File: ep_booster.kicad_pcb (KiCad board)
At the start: 2 copper layers, 37.7 x 25.1 mm, 28 parts, among them J1 TB002-500-04BE, Q1 MMBF5457, Q2 BC849C, SW1 SW_DIP_x02

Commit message: libs and pcb design update (2)
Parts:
- Q1, Q2, R1, R10, R11, R12, R13, R14, R16, R2, R3, R4, R5, R6, R7, R8, R9: moved to B.Cu
- moved R12 30.5 mm to (212.4, 89.4), turned to -90 degrees
- moved R16 27.1 mm to (209.8, 89.4), turned to -90 degrees
- moved R6 26.6 mm to (212.4, 95.4), turned to -90 degrees
- moved R4 25.2 mm to (197.6, 83.2), turned to 0 degrees
- moved R9 24.0 mm to (200.0, 93.0)
- moved C5 21.2 mm to (208.5, 85.0)
- moved R5 18.8 mm to (205.8, 94.4), turned to 180 degrees
- moved R7 15.9 mm to (205.8, 97.0)
- moved C3 15.8 mm to (208.5, 81.8), turned to 180 degrees
- moved C4 15.5 mm to (190.8, 79.8), turned to -90 degrees
- moved Q1 15.3 mm to (187.4, 80.8), turned to -90 degrees
- moved R3 14.8 mm to (200.0, 90.4), turned to 180 degrees
- moved R10 14.0 mm to (197.6, 80.4)
- moved C8 10.5 mm to (192.6, 87.2), turned to 0 degrees
- moved C6 10.4 mm to (186.0, 85.4)
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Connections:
- J1 pad 1: GND -> /IN
- J1 pad 2: Net-(D1-A) -> /OUT
- J1 pad 3: /IN -> Net-(D1-A)
- J1 pad 4: /OUT -> GND
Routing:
- net Net-(Q1-G): track 0.00 -> 31.6 mm
- net VA: track 0.00 -> 31.5 mm
- net Net-(Q2-B): track 0.00 -> 29.1 mm, vias 0 -> 1
- net /IN: track 0.00 -> 20.4 mm
- net Net-(C3-Pad2): track 0.00 -> 20.2 mm, vias 0 -> 1
- net GND: track 0.00 -> 18.1 mm
- net Net-(R16-Pad1): track 0.00 -> 14.4 mm
- net Net-(R3-Pad1): track 0.00 -> 13.8 mm, vias 0 -> 1
- net /OUT: track 0.00 -> 9.08 mm
- net Net-(Q2-E): track 0.00 -> 8.96 mm
- net Net-(C6-Pad2): track 0.00 -> 8.50 mm
- net VB: track 0.00 -> 8.30 mm
- net Net-(C8-Pad2): track 0.00 -> 7.19 mm
- net Net-(Q1-S): track 0.00 -> 5.72 mm
- net Net-(C4-Pad2): track 0.00 -> 5.62 mm
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
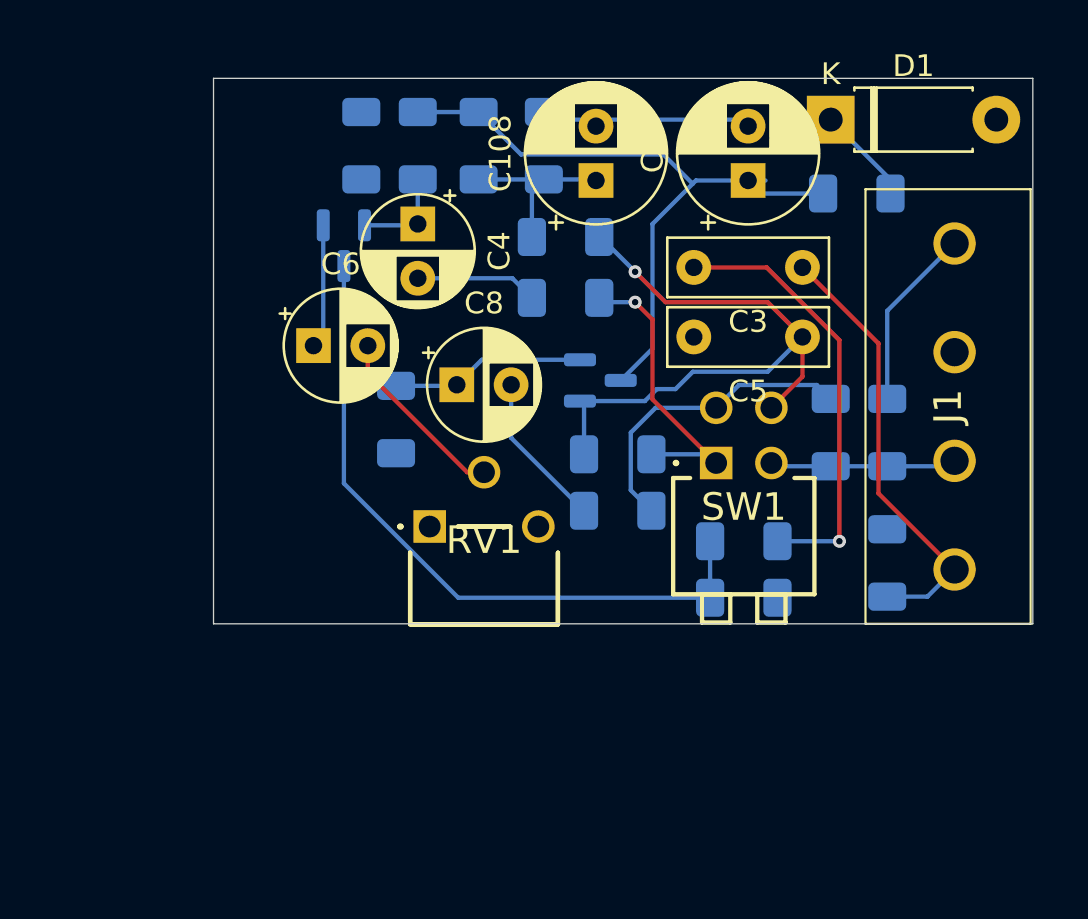
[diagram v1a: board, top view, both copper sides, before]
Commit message: changed pot to bourns 3362S
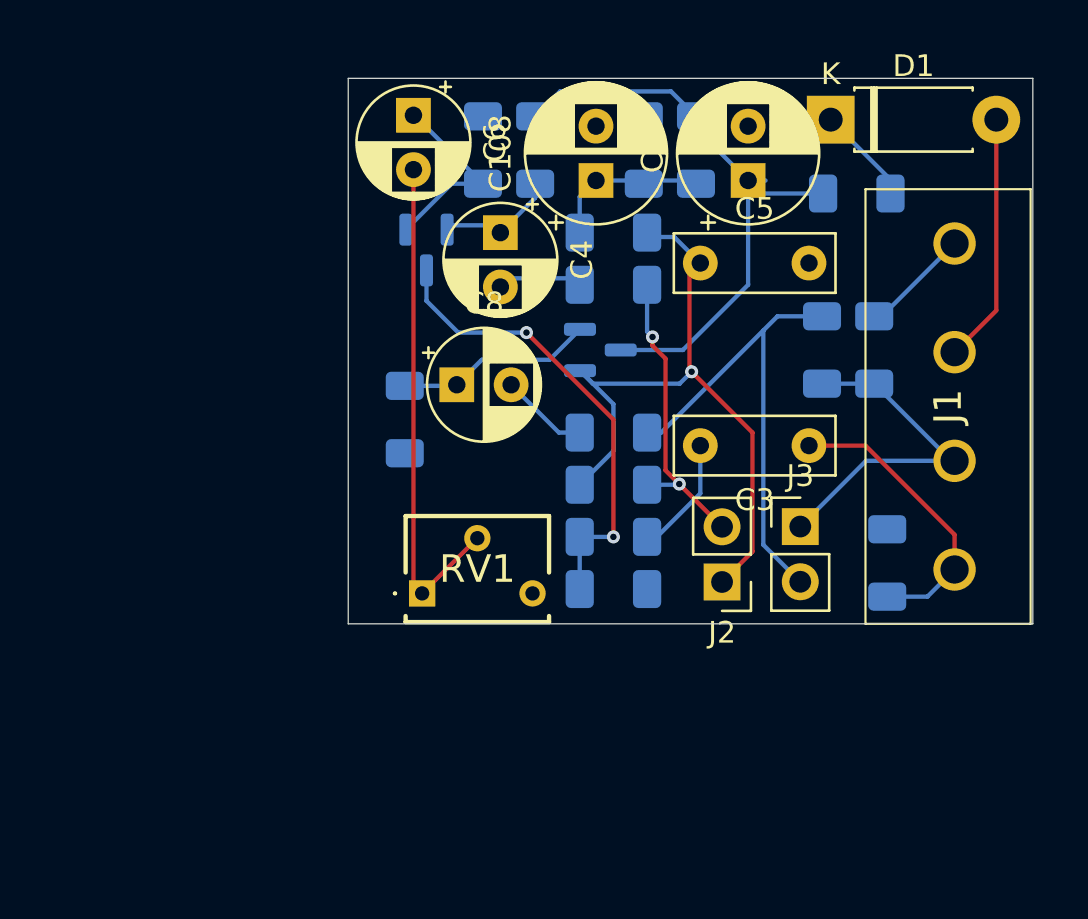
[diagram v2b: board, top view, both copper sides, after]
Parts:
- removed SW1: SW_DIP_x02, DS03-254-02BE:DS0325402BE
- added J2: Conn_01x02_Pin, Connector_PinHeader_2.54mm:PinHeader_1x02_P2.54mm_Vertical, F.Cu at (204.8, 96.3)
- added J3: Conn_01x02_Pin, Connector_PinHeader_2.54mm:PinHeader_1x02_P2.54mm_Vertical, F.Cu at (208.4, 93.7)
- RV1: footprint milos.garunovic:mg_3306K1103 -> footprints:3362S1103LF
- moved C6 11.6 mm to (190.6, 74.8), turned to -90 degrees
- moved R13 10.0 mm to (203.6, 76.4)
- moved C3 8.21 mm to (208.8, 90.0)
- moved R7 6.01 mm to (199.8, 96.6)
- moved R5 6.00 mm to (199.8, 94.2)
- moved C5 5.80 mm to (203.8, 81.6), turned to 0 degrees
- moved R8 5.60 mm to (193.8, 76.4)
- moved R2 5.40 mm to (196.2, 76.4)
- moved R14 4.60 mm to (201.2, 76.4)
- moved R12 3.85 mm to (211.8, 85.6)
- moved R16 3.82 mm to (209.4, 85.6)
- moved C4 3.82 mm to (194.6, 80.2)
- moved Q1 3.81 mm to (191.2, 81.0)
- moved R9 3.61 mm to (199.8, 89.4)
- moved RV1 3.09 mm to (191.0, 96.8)
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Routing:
- net Net-(C6-Pad2): track 8.50 -> 23.3 mm
- net Net-(C3-Pad2): track 20.2 -> 5.48 mm, vias 1 -> 0
- net GND: track 18.1 -> 5.51 mm
- net Net-(D1-A): track 0.00 -> 11.5 mm
- net Net-(Q1-G): track 31.6 -> 21.6 mm, vias 0 -> 2
- net Net-(J3-Pin_2): track 14.4 -> 22.5 mm
- net /OUT: track 9.08 -> 16.1 mm
- net /IN: track 20.4 -> 13.6 mm
- net Net-(Q1-S): track 5.72 -> 8.93 mm
- net Net-(C8-Pad2): track 7.19 -> 4.07 mm
- net VA: track 31.5 -> 28.7 mm
- net Net-(J2-Pin_1): track 29.1 -> 31.8 mm
- net Net-(C4-Pad2): track 5.62 -> 3.94 mm
- net Net-(Q1-D): track 4.53 -> 5.59 mm
- net VB: track 8.30 -> 7.58 mm
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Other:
- board size 37.7 x 25.1 mm -> 31.5 x 25.1 mm

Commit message: component placement update
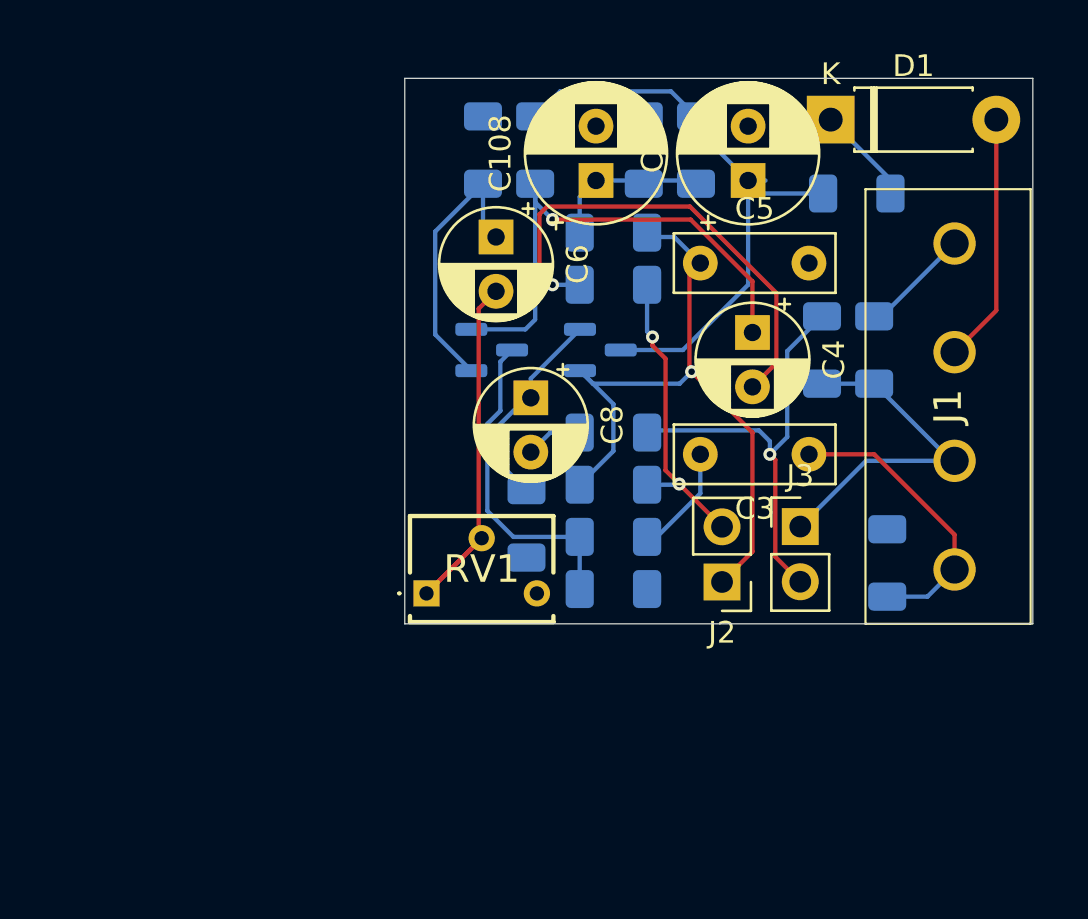
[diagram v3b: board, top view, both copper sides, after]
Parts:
- moved C4 12.5 mm to (206.2, 84.8)
- moved R11 7.38 mm to (195.8, 93.6)
- moved C6 6.77 mm to (194.4, 80.4)
- moved Q1 5.49 mm to (194.2, 85.6), turned to 0 degrees
- moved C8 3.46 mm to (196.0, 87.8), turned to -90 degrees
- moved C3 0.40 mm to (208.8, 90.4)
- moved RV1 0.20 mm to (191.2, 96.8)
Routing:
- net Net-(Q1-D): track 5.59 -> 24.1 mm, vias 0 -> 1
- net Net-(C4-Pad2): track 3.94 -> 22.2 mm, vias 0 -> 1
- net Net-(Q1-G): track 21.6 -> 15.0 mm, vias 2 -> 0
- net Net-(C6-Pad2): track 23.3 -> 18.8 mm
- net Net-(Q1-S): track 8.93 -> 12.9 mm
- net Net-(J3-Pin_2): track 22.5 -> 20.3 mm, vias 0 -> 1
- net Net-(C8-Pad2): track 4.07 -> 2.62 mm
- net Net-(Q2-E): track 9.14 -> 9.70 mm
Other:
- board size 31.5 x 25.1 mm -> 28.9 x 25.1 mm

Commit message: added 9v battery outline on User.1 layer for reference
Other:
- board text added: "9v battery (26x48.3mm or x45.6 without contacts)"
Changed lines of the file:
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@@
 	)
 	(paper "A4")
+	(title_block
+		(title "EP Booster")
+		(date "2025-02-23")
+		(rev "1.0.0")
+		(company "Miloš Garunović")
+	)
 	(layers
 		(0 "F.Cu" signal)
@@
 		(tags "SOT TO_SOT_SMD")
 		(property "Reference" "Q1"
-			(at 0 2.4 360)
+			(at 0 2.4 0)
 			(layer "B.SilkS")
 			(effects
@@
 		)
 		(property "Value" "MMBF5457"
-			(at 0 -2.4 360)
+			(at 0 -2.4 0)
 			(layer "B.Fab")
 			(effects
@@
 		)
 		(property "Footprint" "Package_TO_SOT_SMD:SOT-23"
-			(at 0 0 360)
+			(at 0 0 0)
 			(layer "B.Fab")
 			(hide yes)
@@
 		)
 		(property "Datasheet" "https://www.nxp.com/docs/en/data-sheet/BF545A_BF545B_BF545C.pdf"
-			(at 0 0 360)
+			(at 0 0 0)
 			(layer "B.Fab")
 			(hide yes)
@@
 		)
 		(property "Description" "15mA Idss, 30V Vgs, N-Channel JFET, SOT-23"
-			(at 0 0 360)
+			(at 0 0 0)
 			(layer "B.Fab")
 			(hide yes)
@@
 		)
 		(fp_text user "${REFERENCE}"
-			(at 0 0 360)
+			(at 0 0 0)
 			(layer "B.Fab")
 			(effects
@@
 		(layer "Edge.Cuts")
 	)
+	(gr_line
+		(start 216.6 103.2)
+		(end 216.6 129.2)
+		(stroke
+			(width 0.1)
+			(type default)
+		)
+		(layer "User.1")
+	)
+	(gr_rect
+		(start 171 103.2)
+		(end 219.2 129.2)
+		(stroke
+			(width 0.1)
+			(type default)
+		)
+		(fill none)
+		(layer "User.1")
+	)
+	(gr_text "9v battery (26x48.3mm or x45.6 without contacts)"
+		(at 174.6 117 0)
+		(layer "User.1")
+		(effects
+			(font
+				(size 1 1)
+				(thickness 0.15)
+			)
+			(justify left bottom)
+		)
+	)
 	(dimension
 		(type aligned)
@@
 		(net 18)
 	)
+	(group ""
+		(members "261b35a1-7a30-4973-b5ba-611dcd095195" "29983538-1f1f-49ec-ac33-7b428cfeea65"
+			"8c563be5-e633-4922-b9db-092c95e25ff8"
+		)
+	)
 )

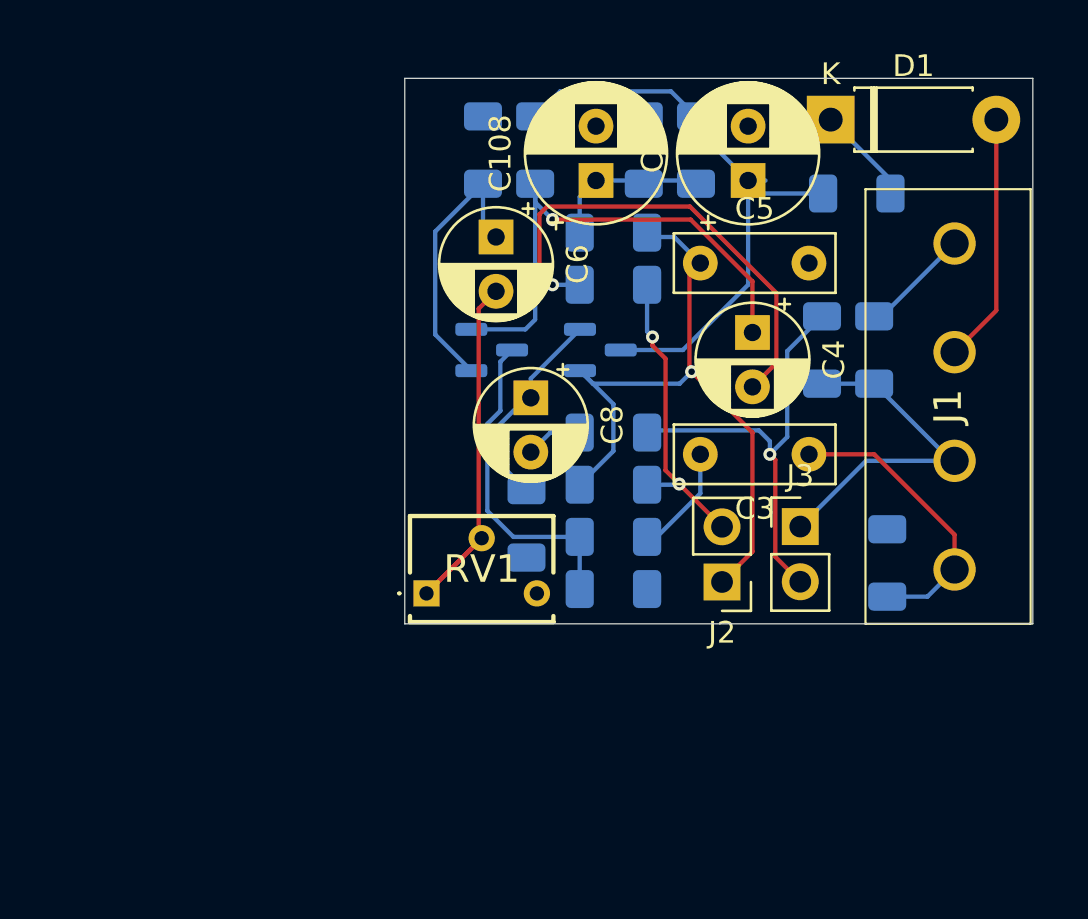
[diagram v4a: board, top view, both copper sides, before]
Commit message: refactored layout and added 2 mounting holes for M3 screws
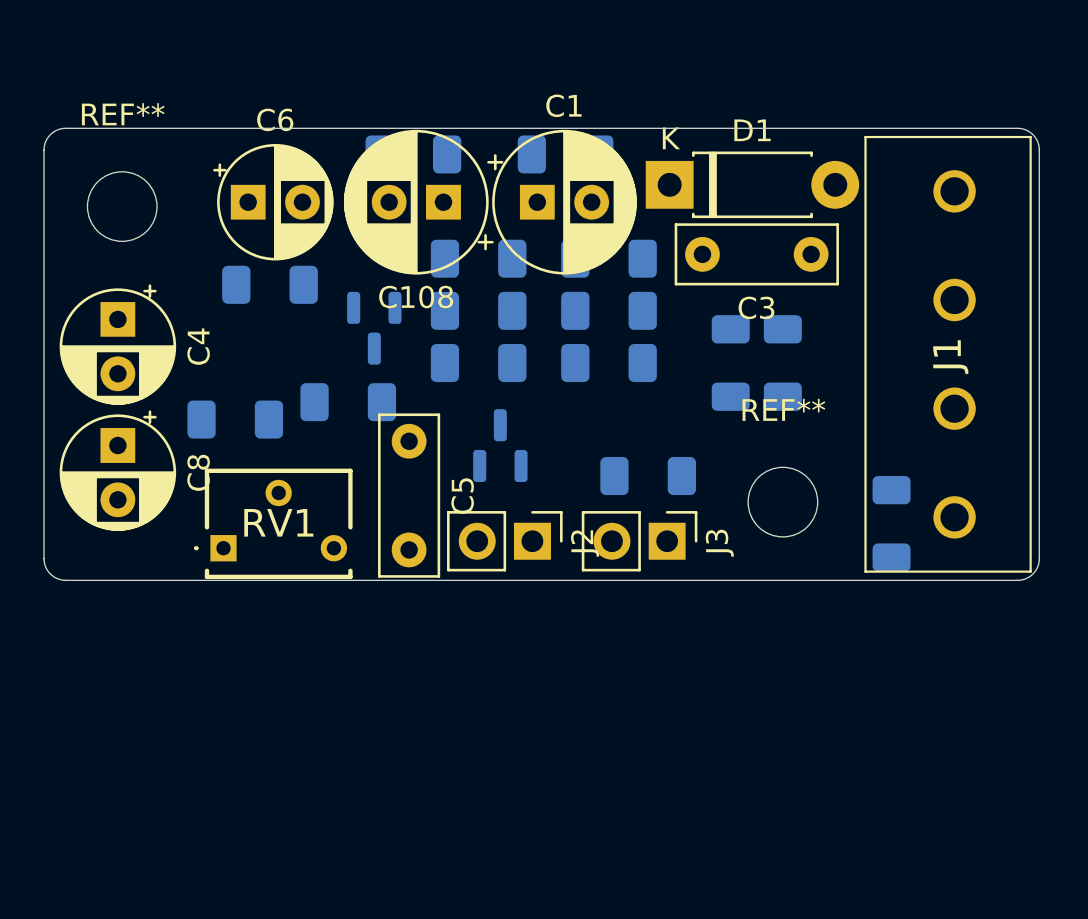
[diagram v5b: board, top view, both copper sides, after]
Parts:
- added REF**: MountingHole_3.2mm_M3, MountingHole:MountingHole_3.2mm_M3, F.Cu at (177.2, 79.0)
- added REF**: MountingHole_3.2mm_M3, MountingHole:MountingHole_3.2mm_M3, F.Cu at (207.6, 92.6)
- moved C4 29.2 mm to (177.0, 84.2)
- moved C8 19.1 mm to (177.0, 90.0)
- moved C5 15.7 mm to (190.4, 89.8), turned to -90 degrees
- moved R11 14.2 mm to (182.4, 88.8), turned to 0 degrees
- moved R1 13.5 mm to (197.6, 76.6)
- moved R4 13.3 mm to (187.6, 88.0)
- moved R5 12.8 mm to (199.6, 81.4)
- moved R7 12.8 mm to (199.6, 83.8)
- moved R8 11.6 mm to (184.0, 82.6), turned to 180 degrees
- moved C6 11.5 mm to (183.0, 78.8), turned to 0 degrees
- moved R13 11.2 mm to (193.6, 81.4), turned to 180 degrees
- moved R14 10.6 mm to (190.6, 76.6), turned to 180 degrees
- moved C1 9.75 mm to (196.3, 78.8), turned to 0 degrees
- moved RV1 9.57 mm to (181.9, 94.7)
- moved C3 9.20 mm to (208.9, 81.2)
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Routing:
- net Net-(J2-Pin_1): track 31.8 -> 0.00 mm, vias 1 -> 0
- net VA: track 28.7 -> 0.00 mm
- net Net-(Q1-D): track 24.1 -> 0.00 mm, vias 1 -> 0
- net Net-(C4-Pad2): track 22.2 -> 0.00 mm, vias 1 -> 0
- net Net-(J3-Pin_2): track 20.3 -> 0.00 mm, vias 1 -> 0
- net Net-(C6-Pad2): track 18.8 -> 0.00 mm
- net /OUT: track 16.1 -> 0.00 mm
- net Net-(Q1-G): track 15.0 -> 0.00 mm
- net Net-(J2-Pin_2): track 14.1 -> 0.00 mm, vias 2 -> 0
- net /IN: track 13.5 -> 0.00 mm
- net Net-(Q1-S): track 12.9 -> 0.00 mm
- net Net-(D1-A): track 11.5 -> 0.00 mm
- net Net-(Q2-E): track 9.70 -> 0.00 mm
- net VB: track 7.58 -> 0.00 mm
- net GND: track 5.51 -> 0.00 mm
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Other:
- board size 28.9 x 25.1 mm -> 45.8 x 20.8 mm

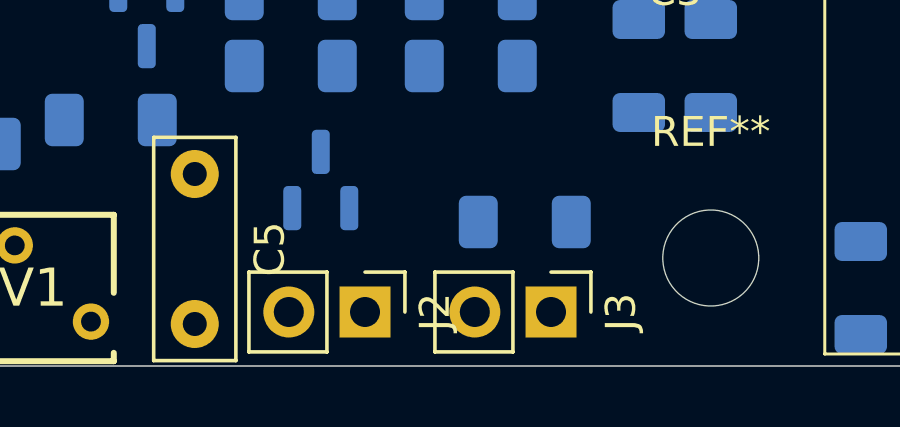
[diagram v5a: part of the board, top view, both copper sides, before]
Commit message: replaced two 1x02 pin headers with 1x04
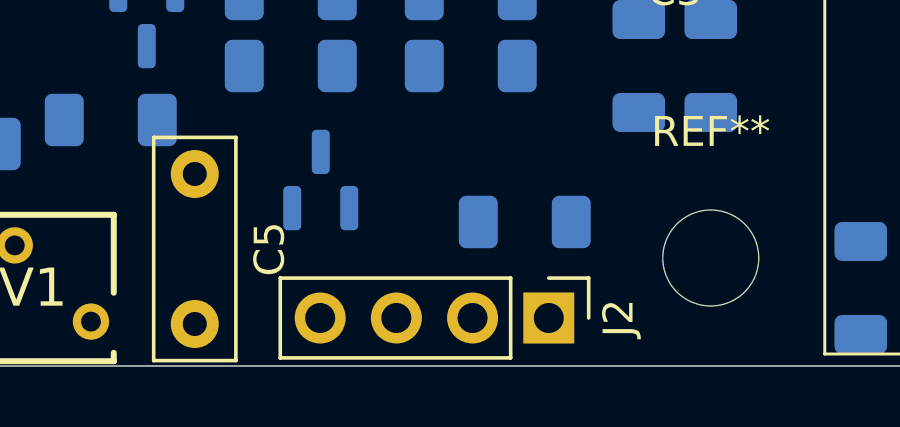
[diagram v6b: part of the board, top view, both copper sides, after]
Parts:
- removed J3: Conn_01x02_Pin, Connector_PinHeader_2.54mm:PinHeader_1x02_P2.54mm_Vertical
- J2: value Conn_01x02_Pin -> Conn_01x04_Pin; footprint Connector_PinHeader_2.54mm:PinHeader_1x02_P2.54mm_Vertical -> Connector_PinHeader_2.54mm:PinHeader_1x04_P2.54mm_Vertical
- moved J2 6.13 mm to (202.2, 94.6)
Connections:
- C5 pad 1: Net-(J2-Pin_1) -> /BRIGHT2
- J2 pad 1: Net-(J2-Pin_1) -> /OUT
- Q2 pad 1: Net-(J2-Pin_1) -> /BRIGHT2
- R10 pad 2: Net-(J2-Pin_1) -> /BRIGHT2
- R16 pad 1: Net-(J3-Pin_2) -> Net-(J2-Pin_2)
- R3 pad 1: Net-(J2-Pin_2) -> /BRIGHT1
- R3 pad 2: Net-(J2-Pin_1) -> /BRIGHT2
- R4 pad 2: Net-(J2-Pin_2) -> /BRIGHT1
- R9 pad 2: Net-(J3-Pin_2) -> Net-(J2-Pin_2)
